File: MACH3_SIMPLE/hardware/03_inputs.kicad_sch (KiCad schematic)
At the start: 33 parts, among them J2 LPT PORT 2, J20 EMG C A Z Y X, J30 MPG handwheel, U10 PC847, U11 PC847, U3 74HC4053

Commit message: MACH3-SIMPLE A1: on-board 5 V, isolated VFD port, four A0 fixes
Power: the 5 V input terminal is gone. An LM2596S-5.0 buck makes +5V from
V24, and the whole supply sits in the top-right corner beside the 24 V
terminal, away from the MCU crystal and the port lines.

Spindle: new J5 (AVI ACM FWD REV DCM). Port 2 pins 7/8/9 go through a
74HC14 to a PC847; the VFD side runs from a B2412S isolated module with a
78L05 reference, a two-pole RC filter and an LM358 trimmed to 10.0 V. It
has its own SP_ACM pour, and the board is routed in two passes so no
board-side copper enters it; autoroute.py barrier checks that and fab.sh
refuses Gerbers without it.

Fixes to A0:
- Q1-Q6 had drain and source swapped; every relay was stuck on through
  the body diode. check_design.py now checks MOSFET orientation.
- The top-edge legends were reversed (+24 over 0V, +5 over MPG B, EMG over
  X home). Signals now follow the printed order, one word per screw.
- PC847 was on a SOIC-16 footprint no PC847 fits; now SMD DIP-16.
- The promised reverse diodes across the input opto LEDs were missing;
  added as D20-D25, with the input channels laid out per screw.

ERC 0, structural checks pass, DRC 0 errors / 0 unconnected / 0 parity,
barrier clean. Not built or powered.

Co-Authored-By: Claude Opus 5.5 <noreply@anthropic.com>
Claude-Session: https://claude.ai/code/session_01MByiLT2xCcbGPkgCYQy33q
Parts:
- added D20, D21, D22, D23, D24, D25: 1N4148 LED reverse, Diode_SMD:D_SOD-123, symbol Device:D
- U10, U11: footprint Package_SO:SOIC-16_3.9x9.9mm_P1.27mm -> Package_DIP:SMDIP-16_W9.53mm
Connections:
- net +5V: now also J30.4 (Pin_4); no longer J30.1 (Pin_1)
- net A_HOME_F: now also J20.4 (Pin_4); no longer J20.3 (Pin_3)
- net A_HOME_LED: now also U10.3, D22.1 (K); no longer U10.5
- net A_HOME_PC: now also U10.14; no longer U10.12
- net C_HOME_F: now also J20.5 (Pin_5); no longer J20.2 (Pin_2)
- net C_HOME_LED: now also U10.5, D21.1 (K); no longer U10.3
- net C_HOME_PC: now also U10.12; no longer U10.14
- net ESTOP_F: now also J20.6 (Pin_6); no longer J20.1 (Pin_1)
- net ESTOP_LED: now also U10.7, D20.1 (K); no longer U10.1
- net ESTOP_PC: now also U10.10; no longer U10.16
- net GND: now also J30.3 (Pin_3), U11.11, U11.6, U11.8, U11.9, D20.2 (A), D21.2 (A), D22.2 (A), D23.2 (A), D24.2 (A), D25.2 (A); no longer J30.2 (Pin_2), U11.13, U11.15, U11.2, U11.4
- net MPG_A_RAW: now also J30.2 (Pin_2); no longer J30.3 (Pin_3)
- net MPG_B_RAW: now also J30.1 (Pin_1); no longer J30.4 (Pin_4)
- net X_HOME_F: now also J20.1 (Pin_1); no longer J20.6 (Pin_6)
- net X_HOME_LED: now also U11.5, D25.1 (K); no longer U11.3
- net X_HOME_PC: now also U11.12; no longer U11.14
- net Y_HOME_F: now also J20.2 (Pin_2); no longer J20.5 (Pin_5)
- net Y_HOME_LED: now also U11.7, D24.1 (K); no longer U11.1
- net Y_HOME_PC: now also U11.10; no longer U11.16
- net Z_HOME_F: now also J20.3 (Pin_3); no longer J20.4 (Pin_4)
- net Z_HOME_LED: now also U10.1, D23.1 (K); no longer U10.7
- net Z_HOME_PC: now also U10.16; no longer U10.10
- net SP_PWM_IN: now reaches J2.7
- net SP_FWD_IN: now reaches J2.8
- net SP_REV_IN: now reaches J2.9
- no-connect marks 22 -> 19

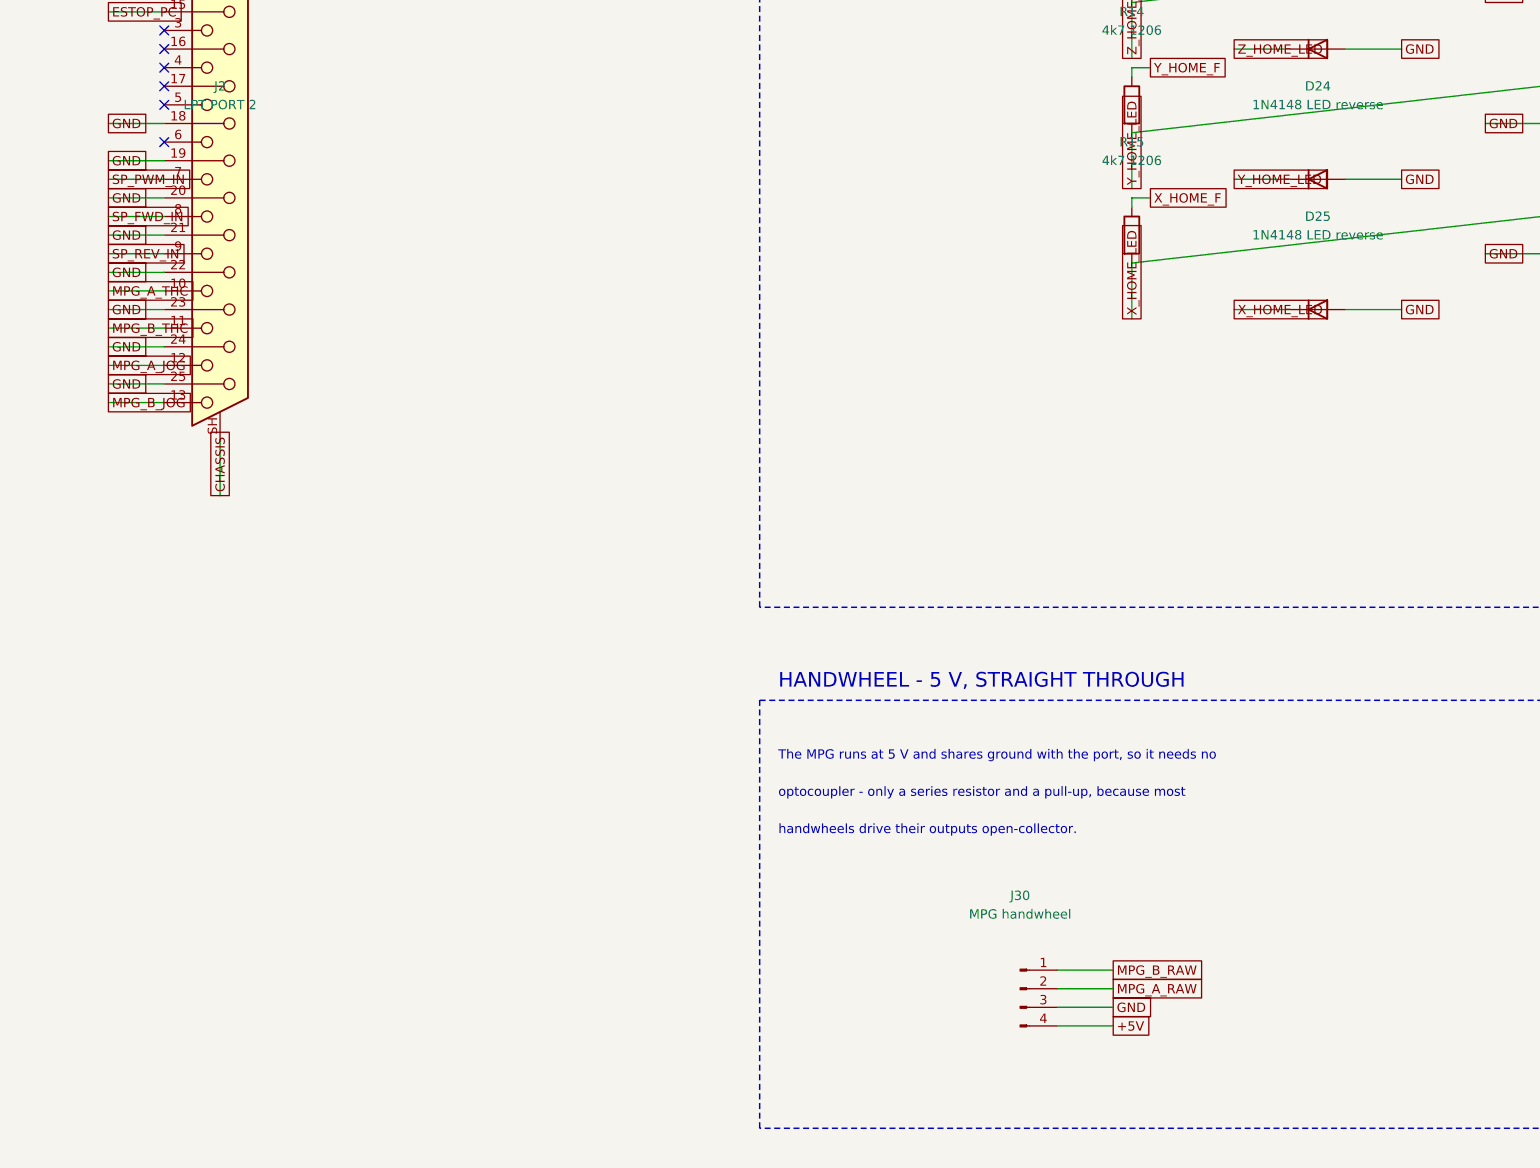
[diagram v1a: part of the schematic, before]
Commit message: MACH3-SIMPLE A1: design-review fixes and options
- Relay terminals labelled: RELAY A-F and NO/COM/NC per screw on the back
  silkscreen, RELAY A-F on the front (were on F.Fab only, not printed).
- R80-R85 4k7 -> 10k: 103 mW in a 100 mW 0603 on 24 V.
- Axis buffers fitted as 74AC245 (same pads) for opto-input drivers.
- J4 is 4-way: fused +24/0V for the sensors beside +24/0V in.
- C2 47 uF 50 V: 100 uF 50 V is not made in 6.3 x 7.7.
- Function labels (5V, 24V, SERIAL, A-F, 10V ADJ), test points GND/5V/24V
  and ACM/12V/AVI, dashed ISOLATED line round the VFD side, MCU heading
  moved beside the MCU.
- Buck switch node hand-drawn and locked: 14 mm top layer, no vias.
- F3 200 mA PTC on the handwheel +5V; 10 nF on MCU reset.
- Spare opto channel as VFD AUX output (port 2 pin 6); J5 is 6-way.
- autoroute.py keeps locked tracks through imports; route_one.py for a
  connection the router leaves open.

ERC 0, structural checks pass, DRC 0 errors / 0 unconnected / 0 parity,
barrier clean. Not built or powered.

Co-Authored-By: Claude Opus 5.5 <noreply@anthropic.com>
Claude-Session: https://claude.ai/code/session_01MByiLT2xCcbGPkgCYQy33q
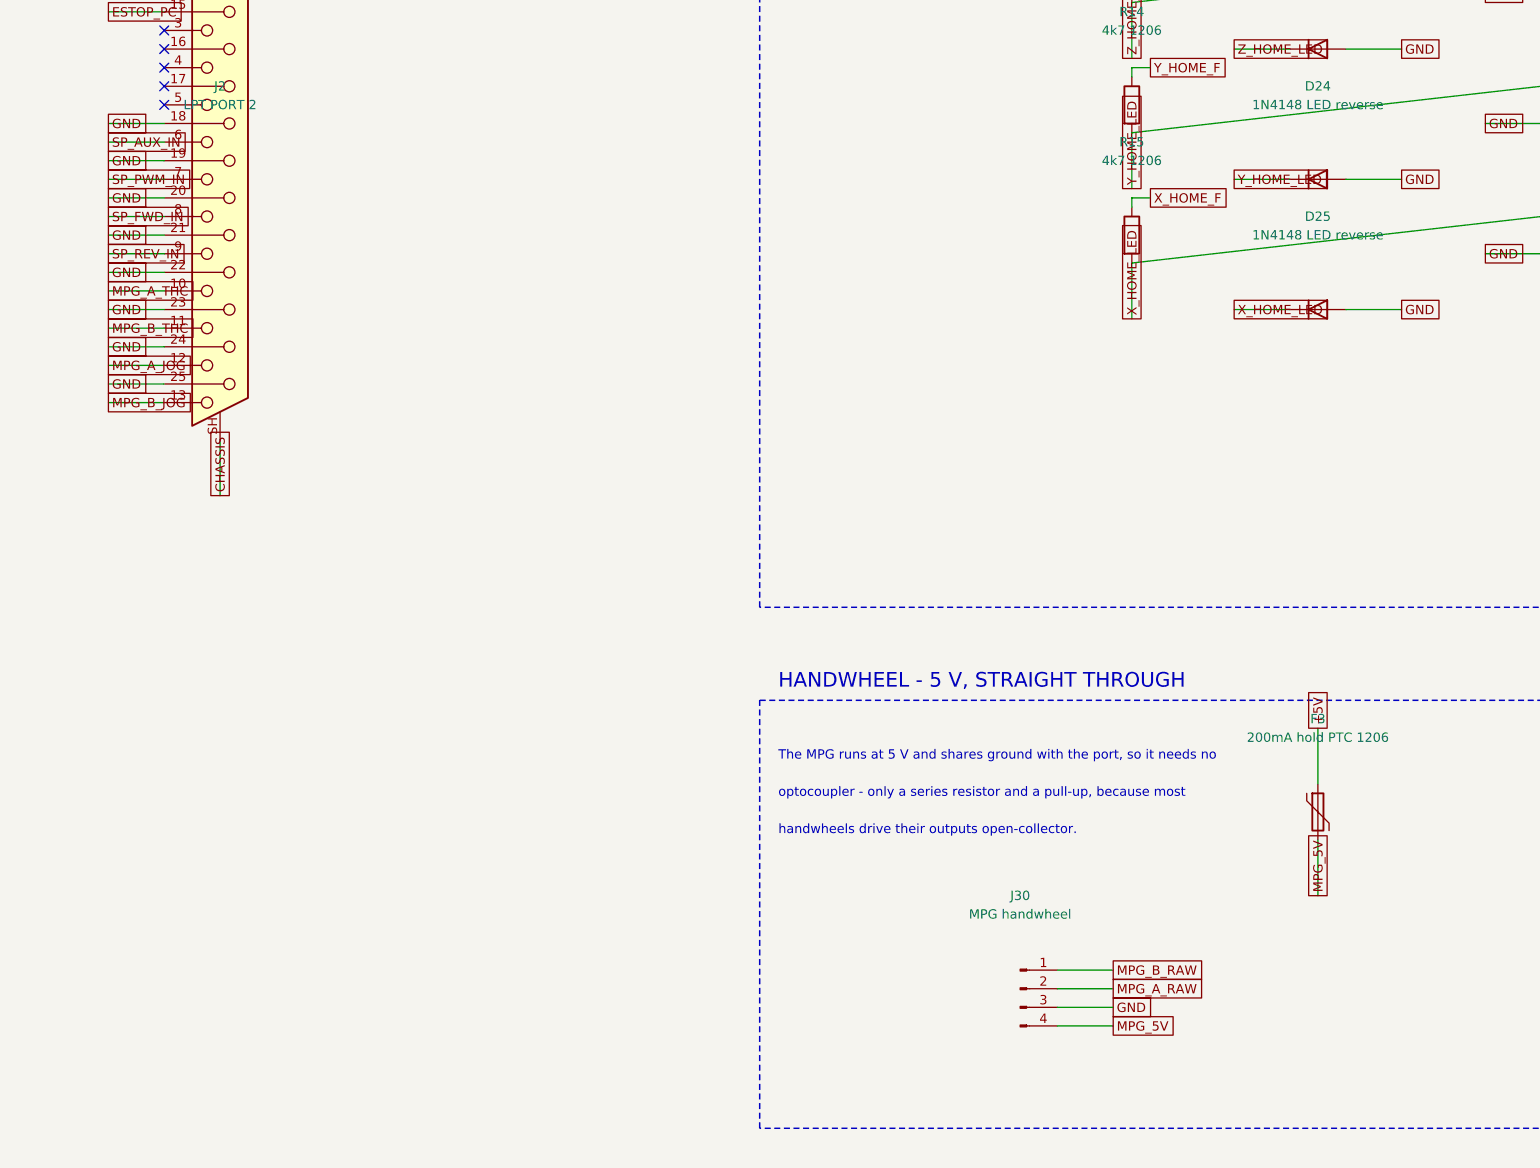
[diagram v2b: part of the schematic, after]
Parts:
- added F3: 200mA hold PTC 1206, Fuse:Fuse_1206_3216Metric, symbol Device:Polyfuse
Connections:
- net +5V: now also F3.1; no longer J30.4 (Pin_4)
- net SP_AUX_IN: now reaches J2.6
- new net MPG_5V: F3.2, J30.4 (Pin_4)
- no-connect marks 19 -> 18
